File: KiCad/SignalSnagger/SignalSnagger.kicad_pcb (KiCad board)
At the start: 4 copper layers, 133.4 x 44.3 mm, 213 parts, among them J102 Left, J104 Right, J105 36-5005-ND, J106 36-5006-ND, J107 36-5006-ND, J108 36-5005-ND, J109 36-5006-ND, J110 36-5006-ND, J203 Conn_01x02, J204 Conn_01x02, J205 DB9 Female, J301 35RASMT2BHSNTRX, J302 36-5005-ND, J303 36-5005-ND, J304 36-5006-ND, P201 ISP/PDI, Q101 MMBT2222A, Q102 MMBT2222A, Q103 MMBT2222A, Q104 MMBT2222A, Q105 MMBT2222A, Q201 BSS84W-7-F, Q202 BSS138W-7-F, SW201 SW_SPST, SW202 SW_SPST, SW203 PEC12R-4225F-S0024, T101 Transformer_1P_SS, U101 74HC74, U102 QS3253QG8, U103 REF4132B33, U104 DG9422E, U105 DG9422E, U201 AVR128DA48, U202 SI5351, U203 LP2985-5.0, U204 LP2985-3.3, U205 EA_DOGS104W-A, U206 LP2985-5.0, U207 MAX1683EUK, U208 TPS22810DBVT, U301 LM386, U302 TS912IDT, U303 TS912IDT, U304 LM386, X201 ECS-327TXO-30-TR, X202 25 MHz

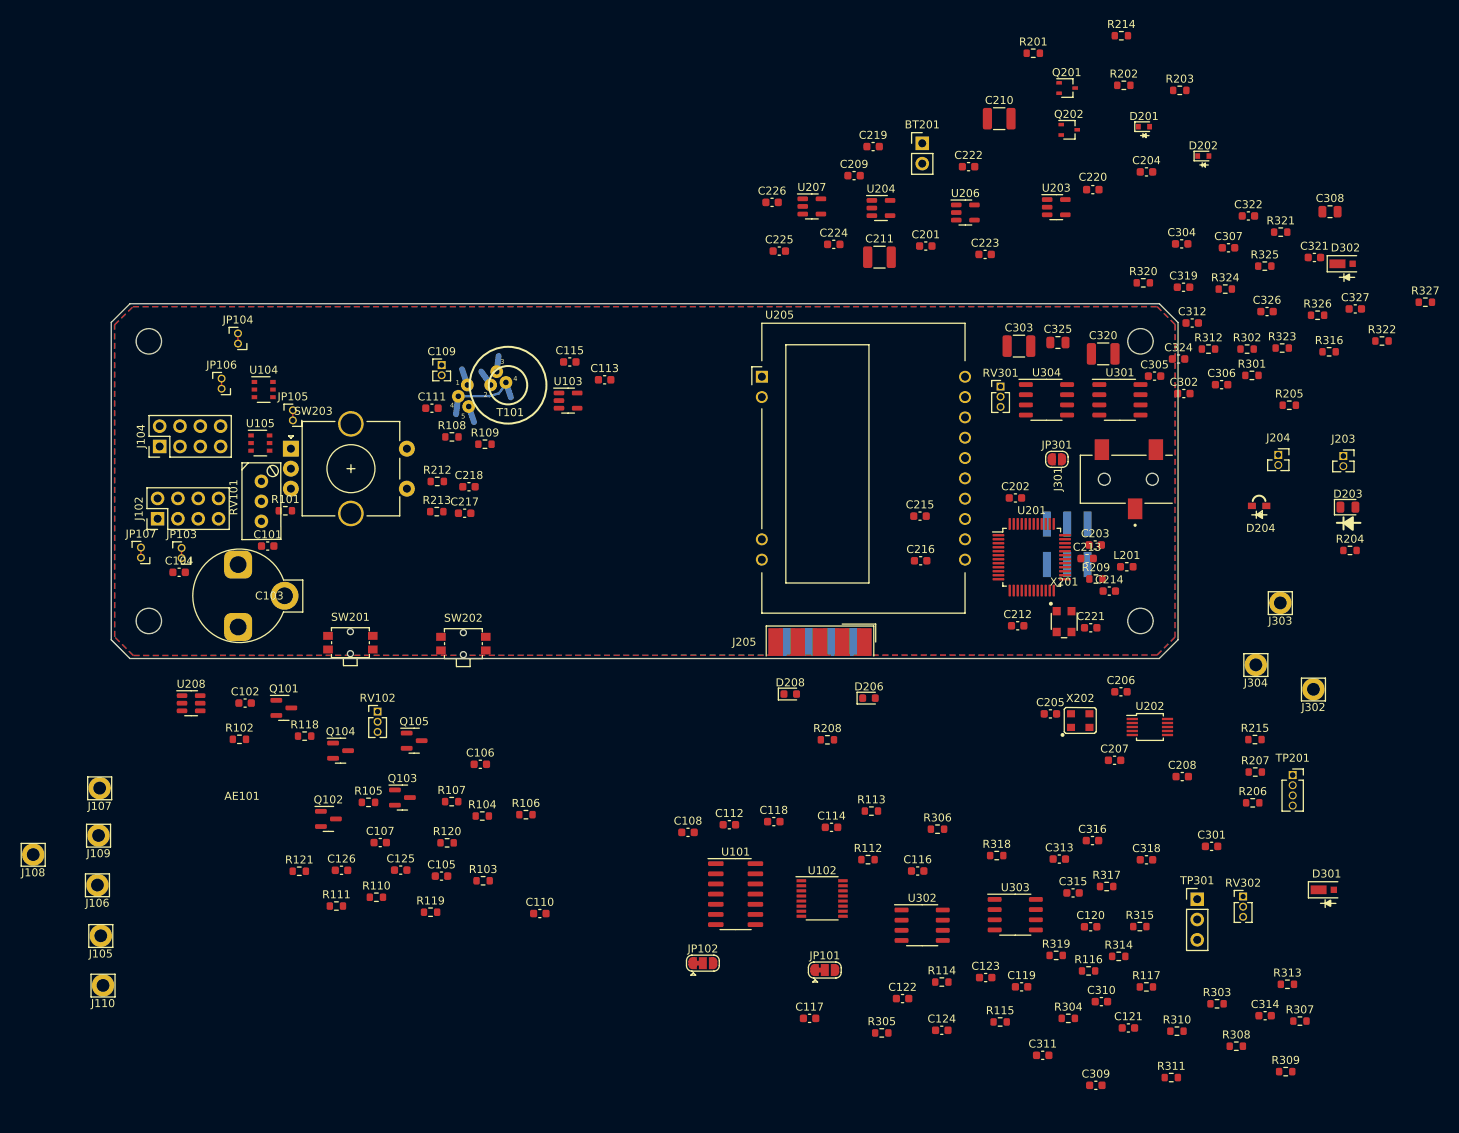
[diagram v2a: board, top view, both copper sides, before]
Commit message: PCB & Schematic Updates
Removed parts not targeted for first prototype
Made other changes discussed in Zoom call
Updated BOM
Updated PCB with new parts list
Noodled with parts placement on PCB
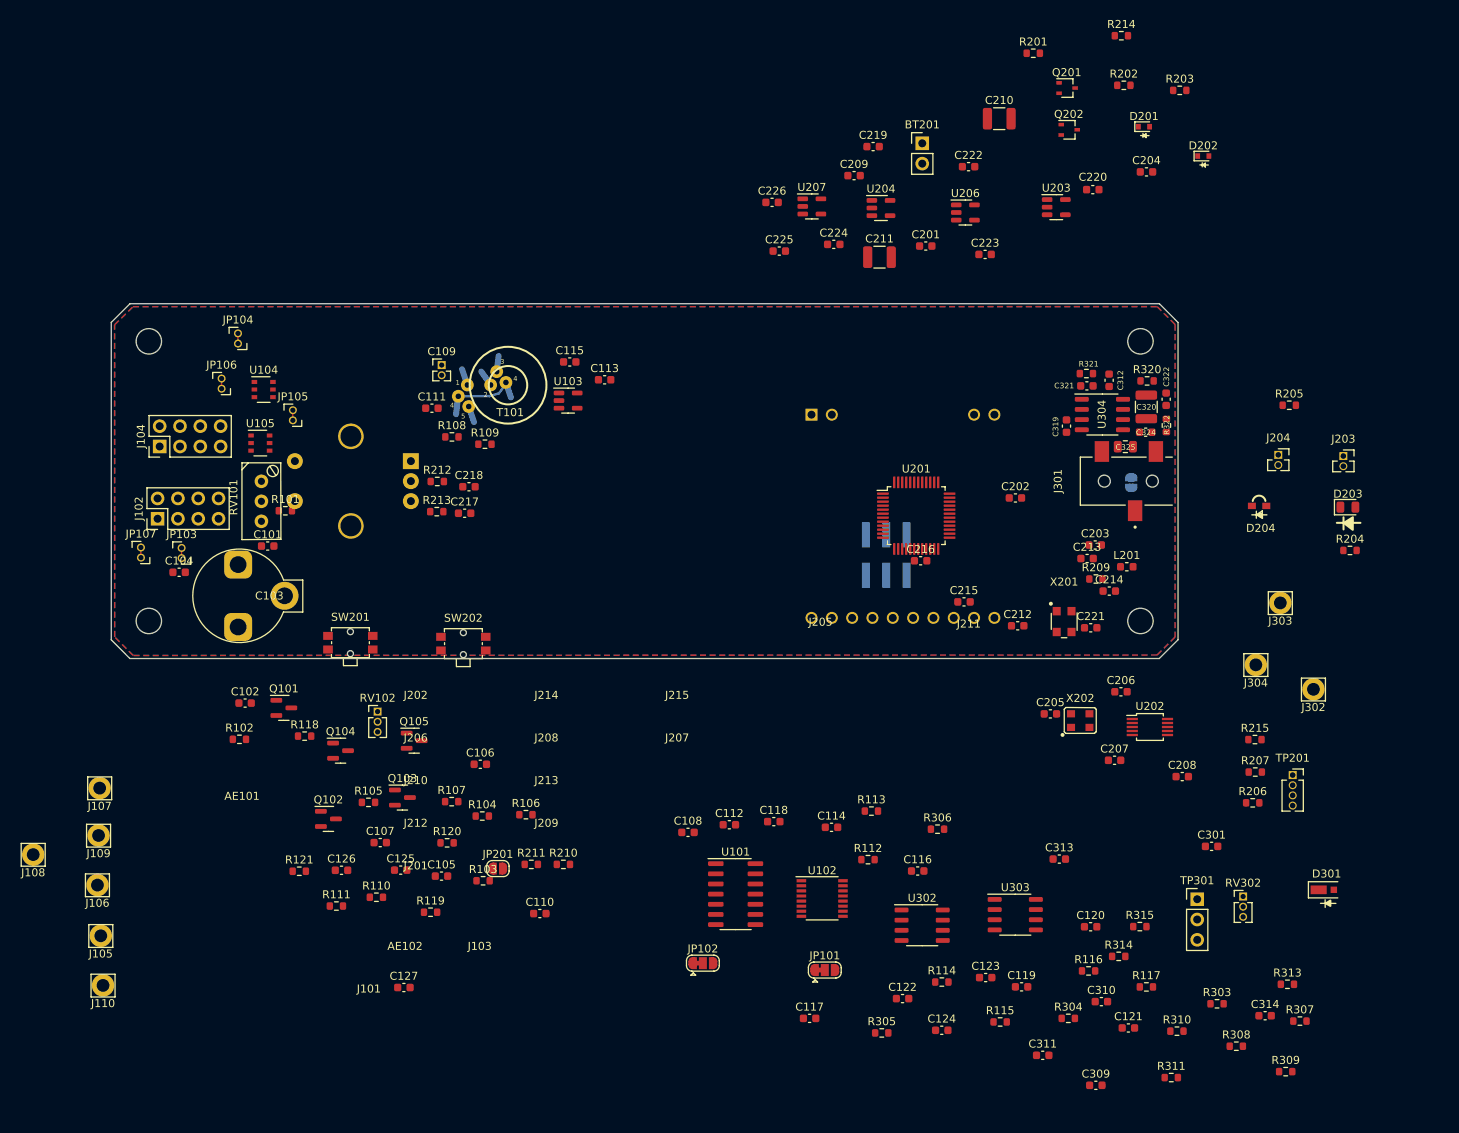
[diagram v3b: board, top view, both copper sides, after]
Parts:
- removed C302: 10nF, Capacitor_SMD:C_0603_1608Metric
- removed C303: 47uF, Capacitor_SMD:C_1210_3225Metric
- removed C304, C307, C318, C326: 100nF, Capacitor_SMD:C_0603_1608Metric
- removed C305, C327: 1uF, Capacitor_SMD:C_0603_1608Metric
- removed C306: 10uF, Capacitor_SMD:C_0603_1608Metric
- removed C308: 22uF, Capacitor_SMD:C_0805_2012Metric
- removed C315: 150nF, Capacitor_SMD:C_0603_1608Metric
- removed C316: 4.7nF, Capacitor_SMD:C_0603_1608Metric
- removed D206, D208: ESD9B5.0ST5G_1, Diode_SMD:D_0603_1608Metric
- removed D302: MSS1P4-M3, Diode_SMD:DO-219AD
- removed R208: 47k, Resistor_SMD:R_0603_1608Metric
- removed R301, R325: 10k, Resistor_SMD:R_0603_1608Metric
- removed R302, R312, R323: 10, Resistor_SMD:R_0603_1608Metric
- removed R316: 470, Resistor_SMD:R_0603_1608Metric
- removed R317: 4.7k, Resistor_SMD:R_0603_1608Metric
- removed R318: 7.5k, Resistor_SMD:R_0603_1608Metric
- removed R319, R327: 51k, Resistor_SMD:R_0603_1608Metric
- removed R324: 330k, Resistor_SMD:R_0603_1608Metric
- removed R326: 1k, Resistor_SMD:R_0603_1608Metric
- removed RV301: 100k, Connector_PinHeader_1.27mm:PinHeader_1x03_P1.27mm_Vertical
- removed U208: TPS22810DBVT, Package_TO_SOT_SMD:SOT-23-6
- removed U301: LM386, Package_SO:SO-8_3.9x4.9mm_P1.27mm
- added AE102: 80m DF Antenna, Oddities:Dummy_Empty, F.Cu at (113.9, 156.8)
- added C127: 100nF, Capacitor_SMD:C_0603_1608Metric, F.Cu at (113.8, 159.5)
- added J101: Left, Oddities:Dummy_Empty, F.Cu at (109.4, 162.1)
- added J103: Right, Oddities:Dummy_Empty, F.Cu at (123.3, 156.8)
- added J201: Conn_01x01_Female, Oddities:Dummy_Empty, F.Cu at (115.3, 146.8)
- added J202: Conn_01x01_Female, Oddities:Dummy_Empty, F.Cu at (115.3, 125.4)
- added J206: Conn_01x01_Female, Oddities:Dummy_Empty, F.Cu at (115.3, 130.8)
- added J207: Conn_01x01_Female, Oddities:Dummy_Empty, F.Cu at (147.9, 130.8)
- added J208: Conn_01x01_Female, Oddities:Dummy_Empty, F.Cu at (131.6, 130.8)
- added J209: Conn_01x01_Female, Oddities:Dummy_Empty, F.Cu at (131.6, 141.4)
- added J210: Conn_01x01_Female, Oddities:Dummy_Empty, F.Cu at (115.3, 136.1)
- added J211: Conn_01x01_Female, Oddities:Dummy_Empty, F.Cu at (184.4, 116.5)
- added J212: Conn_01x01_Female, Oddities:Dummy_Empty, F.Cu at (115.3, 141.4)
- added J213: Conn_01x01_Female, Oddities:Dummy_Empty, F.Cu at (131.6, 136.1)
- added J214: Conn_01x01_Female, Oddities:Dummy_Empty, F.Cu at (131.6, 125.4)
- added J215: Conn_01x01_Female, Oddities:Dummy_Empty, F.Cu at (147.9, 125.4)
- added JP201: SolderJumper_2_Open, Jumper:SolderJumper-2_P1.3mm_Open_RoundedPad1.0x1.5mm, F.Cu at (125.6, 144.6)
- added R210: NP, Resistor_SMD:R_0603_1608Metric, F.Cu at (133.8, 144.1)
- added R211: NP, Resistor_SMD:R_0603_1608Metric, F.Cu at (129.8, 144.1)
- BT201: value Battery -> +7.4V 2S Battery
- C125, C126: value 10uF -> 1uF
- J205: value DB9 Female -> Conn_01x01_Female; footprint Connector_Dsub:DSUB-9_Female_EdgeMount_P2.77mm -> Oddities:Dummy_Empty
- JP301, SW203, U205: moved to B.Cu
- R110, R111: value 4.7k -> 2.7k
- R119: value 1k -> 2.7k
- moved C321 32.7 mm to (199.2, 84.3)
- moved R321 30.0 mm to (199.2, 82.7), turned to 180 degrees
- moved R322 28.9 mm to (209.2, 89.2), turned to 90 degrees
- moved C322 25.1 mm to (209.1, 86.0), turned to 90 degrees
- moved C319 22.7 mm to (196.7, 89.3), turned to -90 degrees
- moved P201 22.7 mm to (174.1, 105.4)
- moved C325 15.5 mm to (204.0, 91.9)
- moved U201 15.3 mm to (177.9, 100.5)
- moved C312 12.6 mm to (202.0, 83.6), turned to -90 degrees
- moved R320 12.3 mm to (206.8, 83.7)
- moved C215 12.0 mm to (183.9, 111.3)
- moved C324 10.0 mm to (206.6, 90.1), turned to 180 degrees
- moved JP301 9.74 mm to (204.8, 96.4), turned to -90 degrees
- moved C320 8.54 mm to (206.7, 86.9), turned to 90 degrees
- moved U205 7.81 mm to (164.8, 87.9), turned to -90 degrees
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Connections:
- Q104 pad 3: Net-(C106-Pad1) -> +10V
- R119 pad 1: Net-(C106-Pad1) -> +10V
- U201 pad 5: Sense_Anable -> /Processor/PB1
- U303 pad 5: Vref -> (no net)
- U303 pad 6: Net-(C315-Pad1) -> (no net)
- U303 pad 7: Net-(C316-Pad1) -> (no net)

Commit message: Ver 0.303
Schematic and PCB updates.
Added R122.
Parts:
- added R122: 10k, Resistor_SMD:R_0603_1608Metric, F.Cu at (128.4, 133.6)
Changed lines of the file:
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@@
+    )
+  )
+  (footprint "Resistor_SMD:R_0603_1608Metric" (layer "F.Cu")
+    (at 128.42 133.56)
+    (descr "Resistor SMD 0603 (1608 Metric), square (rectangular) end terminal, IPC_7351 nominal, (Body size source: IPC-SM-782 page 72, https://www.pcb-3d.com/wordpress/wp-content/uploads/ipc-sm-782a_amendment_1_and_2.pdf), generated with kicad-footprint-generator")
+    (tags "resistor")
+    (property "Description" "RES 10K OHM 1% 1/10W 0603")
+    (property "Digi-Key Part No." "311-10.0KHRCT-ND")
+    (property "Link" "https://www.digikey.com/en/products/detail/yageo/RC0603FR-0710KL/726880")
+    (property "Manufacturer" "YAGEO")
+    (property "Manufacturer PN" "RC0603FR-0710KL")
+    (property "Sheetfile" "SignalSnagger.kicad_sch")
+    (property "Sheetname" "")
+    (attr smd)
+    (fp_text reference "R122" (at 0 -1.43) (layer "F.SilkS")
+      (effects (font (size 1 1) (thickness 0.15)))
+    )
+    (fp_text value "10k" (at 0 1.43) (layer "F.Fab")
+      (effects (font (size 1 1) (thickness 0.15)))
+    )
+    (fp_text user "${REFERENCE}" (at 0 0) (layer "F.Fab")
+      (effects (font (size 0.4 0.4) (thickness 0.06)))
+    )
+    (fp_line (start -0.237258 -0.5225) (end 0.237258 -0.5225) (layer "F.SilkS") (width 0.12))
+    (fp_line (start -0.237258 0.5225) (end 0.237258 0.5225) (layer "F.SilkS") (width 0.12))
+    (fp_line (start 1.48 0.73) (end -1.48 0.73) (layer "F.CrtYd") (width 0.05))
+    (fp_line (start 1.48 -0.73) (end 1.48 0.73) (layer "F.CrtYd") (width 0.05))
+    (fp_line (start -1.48 -0.73) (end 1.48 -0.73) (layer "F.CrtYd") (width 0.05))
+    (fp_line (start -1.48 0.73) (end -1.48 -0.73) (layer "F.CrtYd") (width 0.05))
+    (fp_line (start 0.8 0.4125) (end -0.8 0.4125) (layer "F.Fab") (width 0.1))
+    (fp_line (start -0.8 -0.4125) (end 0.8 -0.4125) (layer "F.Fab") (width 0.1))
+    (fp_line (start -0.8 0.4125) (end -0.8 -0.4125) (layer "F.Fab") (width 0.1))
+    (fp_line (start 0.8 -0.4125) (end 0.8 0.4125) (layer "F.Fab") (width 0.1))
+    (pad "1" smd roundrect (at -0.825 0) (size 0.8 0.95) (layers "F.Cu" "F.Paste" "F.Mask") (roundrect_rratio 0.25)
+      (net 73 "Net-(J109-Pad1)") (pintype "passive"))
+    (pad "2" smd roundrect (at 0.825 0) (size 0.8 0.95) (layers "F.Cu" "F.Paste" "F.Mask") (roundrect_rratio 0.25)
+      (net 1 "GND") (pintype "passive"))
+    (model "${KICAD6_3DMODEL_DIR}/Resistor_SMD.3dshapes/R_0603_1608Metric.wrl"
+      (offset (xyz 0 0 0))
+      (scale (xyz 1 1 1))
+      (rotate (xyz 0 0 0))
     )
   )

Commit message: Ver 0.303
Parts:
- removed J205, J211: Conn_01x01_Female, Oddities:Dummy_Empty
- P201: moved to F.Cu
- moved SW202 46.0 mm to (143.0, 76.0), turned to 180 degrees
- moved SW201 43.0 mm to (122.0, 76.0), turned to 180 degrees
- moved P201 7.09 mm to (167.2, 106.7)

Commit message: Ver 0.304
Schematic fixes
PCB updates
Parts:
- removed AE101: Sense Ant., Oddities:Dummy_Empty
- removed AE102: 80m DF Antenna, Oddities:Dummy_Empty
- removed C108: 100nF, Capacitor_SMD:C_0603_1608Metric
- removed J101: Left, Oddities:Dummy_Empty
- removed J103: Right, Oddities:Dummy_Empty
- removed J201, J202, J206, J207, J208, J209, J210, J212, J213, J214, J215: Conn_01x01_Female, Oddities:Dummy_Empty
- removed JP101, JP102: SolderJumper_3_Bridged12, Jumper:SolderJumper-3_P1.3mm_Bridged12_RoundedPad1.0x1.5mm
- removed R210, R211: NP, Resistor_SMD:R_0603_1608Metric
- removed U101: 74HC74, Package_SO:SO-14_3.9x8.65mm_P1.27mm
- BT201: footprint Connector_PinHeader_2.54mm:PinHeader_1x02_P2.54mm_Vertical -> Connector_Wire:SolderWire-1sqmm_1x02_P7.8mm_D1.4mm_OD3.9mm_Relief; moved to B.Cu
- C103, JP201, TP201: moved to B.Cu
- D204: footprint LED_SMD:LED_APDA1806SECK -> LED_SMD:LED_0805_2012Metric
- RV302: footprint Connector_PinHeader_1.27mm:PinHeader_1x03_P1.27mm_Vertical -> Potentiometer_SMD:Potentiometer_Bourns_TC33X_Vertical
- moved JP201 111.3 mm to (172.4, 43.6), turned to 90 degrees
- moved R212 109.0 mm to (210.8, 153.4), turned to -90 degrees
- moved R215 107.3 mm to (154.9, 43.3)
- moved R213 105.5 mm to (207.7, 155.5), turned to 90 degrees
- moved C217 102.7 mm to (209.2, 153.4), turned to 90 degrees
- moved C218 102.6 mm to (206.1, 155.5), turned to 90 degrees
- moved C113 82.5 mm to (114.2, 162.2), turned to 180 degrees
- moved J303 82.3 mm to (163.6, 167.9)
- moved C115 82.0 mm to (110.9, 159.8), turned to 90 degrees
- moved TP201 76.7 mm to (149.3, 145.6), turned to -90 degrees
- moved U103 76.3 mm to (113.8, 159.6)
- moved R205 73.8 mm to (228.8, 160.3)
- moved T101 73.1 mm to (123.4, 157.2)
- moved C109 71.2 mm to (115.2, 152.8)
- moved C111 70.1 mm to (114.2, 157.1), turned to 180 degrees
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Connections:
- TP201 pad 3: SCL0 -> SDA0
- TP201 pad 4: SDA0 -> SCL0
- U102 pad 14: Net-(JP102-Pad2) -> QSD_CLK0
- U102 pad 2: Net-(JP101-Pad2) -> QSD_CLK1
- U201 pad 6: SDA1 -> /Processor/SDA1
- U201 pad 7: SCL1 -> /Processor/SCL1
- U303 pad 5: (no net) -> Vref
- U303 pad 6: (no net) -> Net-(U303-Pad6)
- U303 pad 7: (no net) -> Net-(U303-Pad6)
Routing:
- added copper zone on B.Cu, net Net-(J102-Pad8)
- added copper zone on F.Cu, net Net-(J102-Pad8)
- added copper zone on In1.Cu, net Net-(J102-Pad8)
- added copper zone on In2.Cu, net Net-(J102-Pad8)
- removed copper zone on B.Cu, net (none)
- removed copper zone on F.Cu, net (none)
- removed copper zone on In1.Cu, net (none)
- removed copper zone on In2.Cu, net (none)
